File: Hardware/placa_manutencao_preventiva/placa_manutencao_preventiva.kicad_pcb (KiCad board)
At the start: 2 copper layers, 58.4 x 120 mm, 41 parts, among them J1 ENT_DIGITAL, J12 Conn_01x01, J13 Conn_01x01, J14 Conn_01x01, J15 Conn_01x01, J16 Conn_01x01, J17 Conn_01x01, J18 Conn_01x01, J19 Conn_01x01, J2 Power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

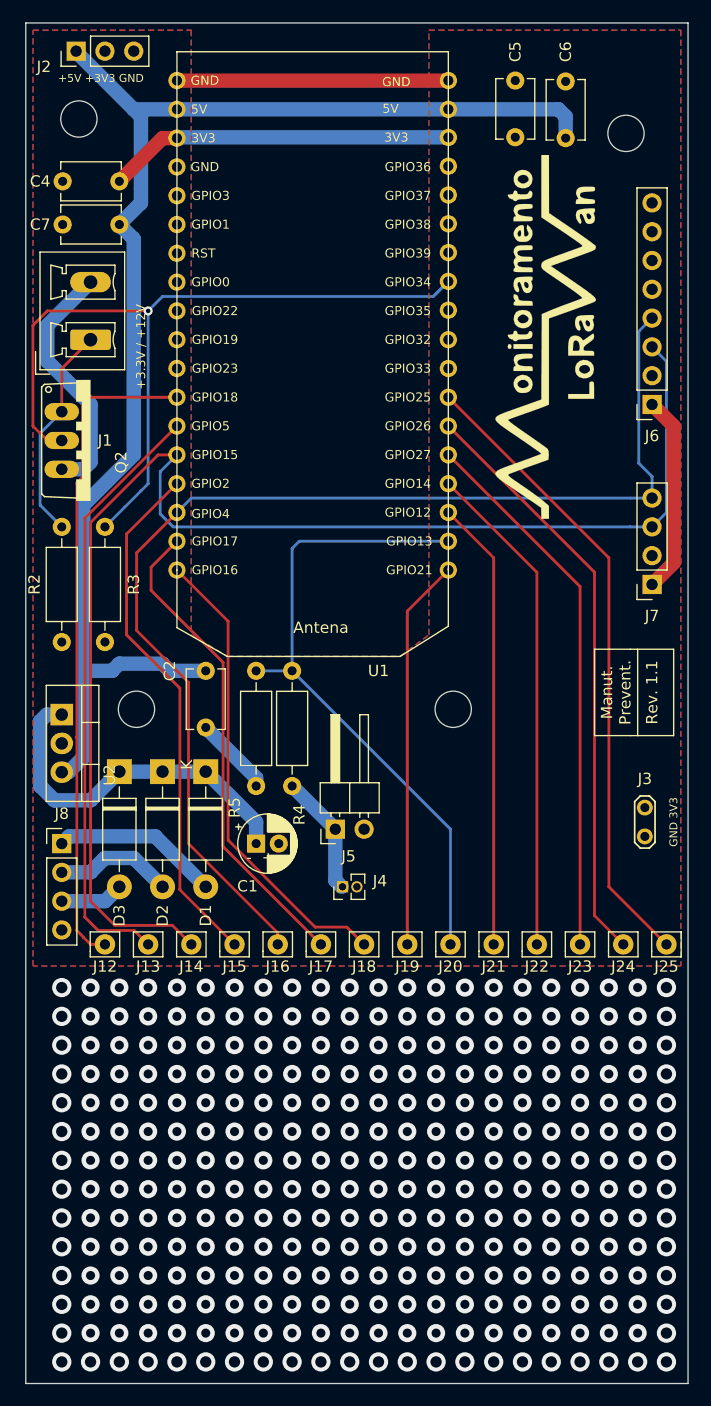
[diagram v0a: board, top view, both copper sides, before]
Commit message: Substituição do mosfet para BSS-89
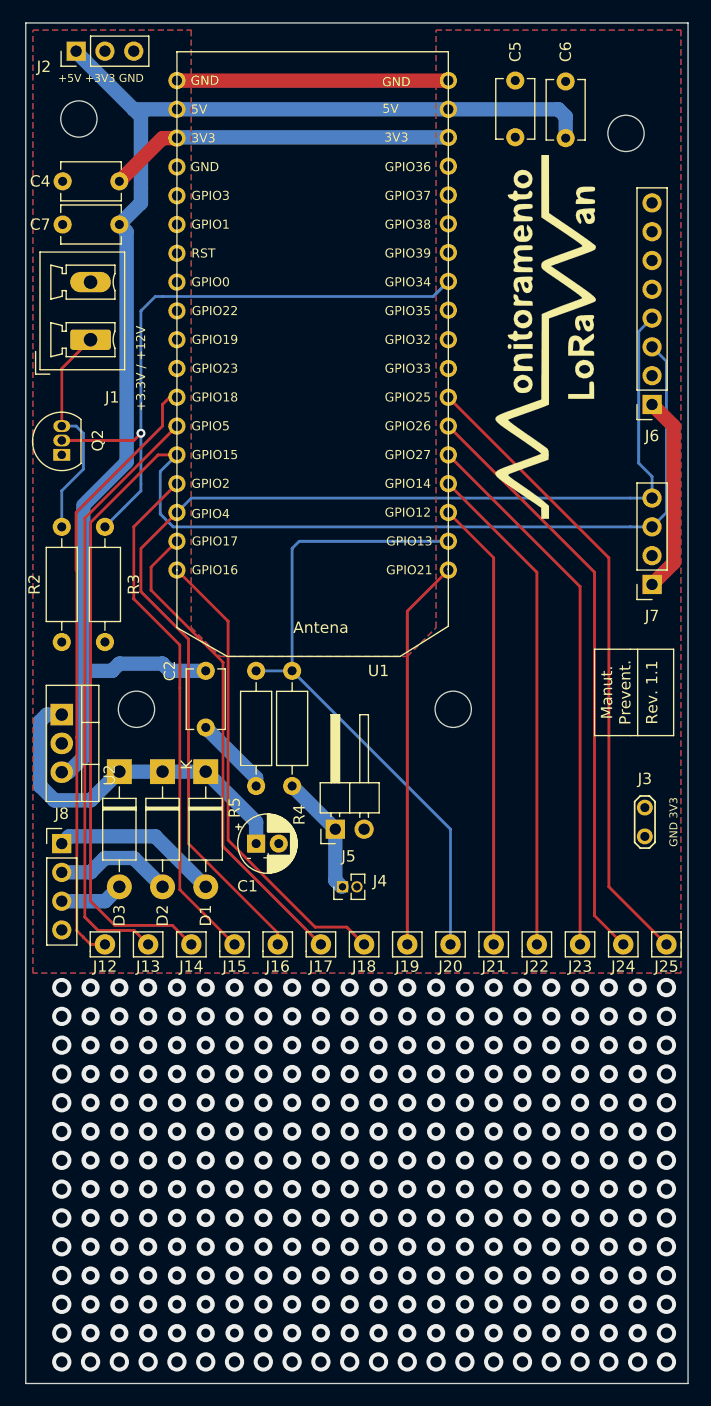
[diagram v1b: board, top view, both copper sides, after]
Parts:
- Q2: value FQP30N06L -> BSS89; footprint fqp30n06l:TO220V -> TO-92L_Inline
- moved Q2 2.84 mm to (81.0, 53.1), turned to 90 degrees
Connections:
- Q2 pad 1: Net-(J1-Pad1) -> GND
- Q2 pad 3: GND -> Net-(J1-Pad1)
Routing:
- net GND: track 53.3 -> 30.9 mm
- net ENT_DIGITAL: track 72.5 -> 57.4 mm
- net Net-(J12-Pad1): track 58.2 -> 54.1 mm
- net Net-(J1-Pad1): track 19.1 -> 19.9 mm
- net Net-(J15-Pad1): track 46.4 -> 45.9 mm
- net +5V: track 123.5 -> 123.0 mm
